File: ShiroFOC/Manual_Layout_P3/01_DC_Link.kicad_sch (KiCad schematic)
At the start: 19 parts, among them J101 AMASS XT60PW-M

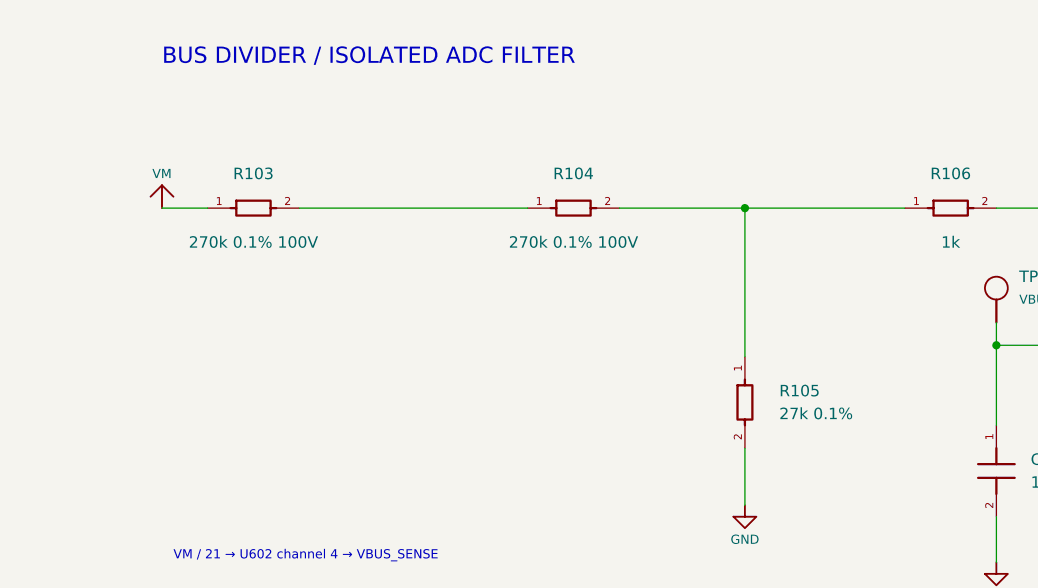
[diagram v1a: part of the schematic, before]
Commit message: STSPIN solder paste updated
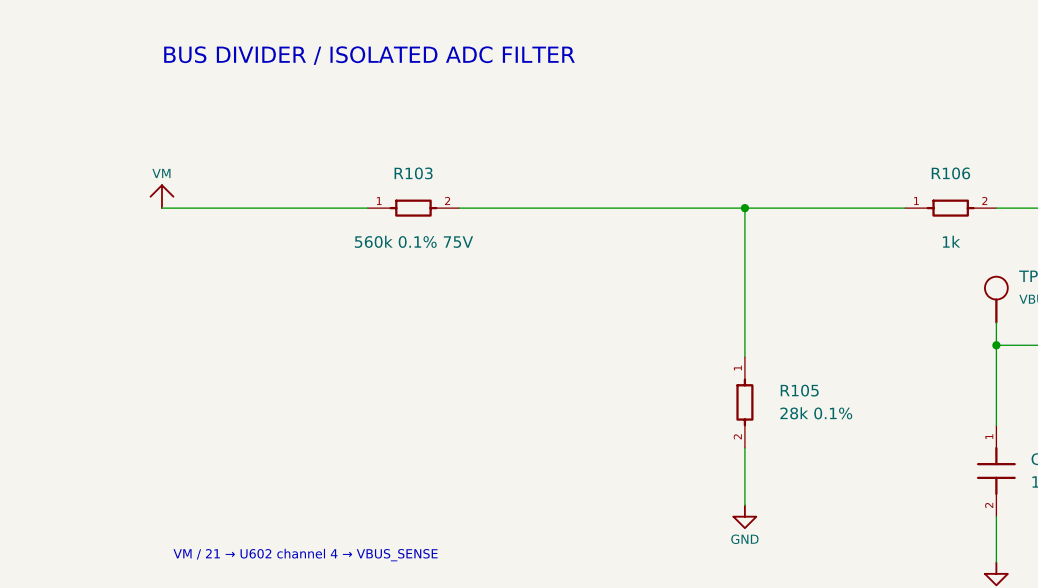
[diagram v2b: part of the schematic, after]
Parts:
- removed R104: 270k 0.1% 100V, Resistor_SMD:R_1206_3216Metric, symbol Manual:COMP_R104
- C108: Selection Note (none) -> ADC filter after U602 isolation. With 560k/28k divider and 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
- R103: value 270k 0.1% 100V -> 560k 0.1% 75V; footprint Resistor_SMD:R_1206_3216Metric -> Resistor_SMD:R_0603_1608Metric; LCSC (none) -> C719312; MPN (none) -> RT0603BRD07560KL; Manufacturer (none) -> Yageo; Procurement Select to specification: 270k 0.1% 100V; R_1206_3216Metric -> RT0603BRD07560KL; 560k 0.1%; 0603; 75V continuous rating; Rating See Value; generic low-voltage passives: R >=0.1 W / 50 V, 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 -> 0.1%; 25ppm/K; 0.1W; 75V continuous; Selection Note (none) -> Single upper resistor replaces R103/R104. Paired with R105=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
- R105: value 27k 0.1% -> 28k 0.1%; LCSC (none) -> C852686; MPN (none) -> RT0402BRD0728KL; Manufacturer (none) -> Yageo; Procurement 0402; preserve Value/tolerance requirements; exact part not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 -> RT0402BRD0728KL; 28k 0.1%; 0402; Rating See Value; generic low-voltage passives: R >=0.1 W / 50 V, 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 -> 0.1%; 25ppm/K; 0.0625W; 50V; Selection Note (none) -> Lower leg for R103=560k; preserves exact nominal division b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
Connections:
- net at R103.2: now also R105.1, R106.1
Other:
- moved on the sheet: R103
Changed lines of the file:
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@@
 	(wire
 		(pts
-			(xy 162.56 119.38) (xy 167.64 119.38)
+			(xy 162.56 119.38) (xy 185.42 119.38)
 		)
 		(stroke
@@
 	(wire
 		(pts
-			(xy 213.36 119.38) (xy 227.33 119.38)
+			(xy 195.58 119.38) (xy 227.33 119.38)
 		)
 		(stroke
@@
 		(pts
 			(xy 124.46 87.63) (xy 157.48 87.63)
-		)
-		(stroke
-			(width 0)
-			(type default)
-		)
-	)
-	(wire
-		(pts
-			(xy 177.8 119.38) (xy 203.2 119.38)
 		)
 		(stroke
@@
 			)
 		)
+		(property "Selection Note" "ADC filter after U602 isolation. With 560k/28k divider and R106=1k: nominal tau 277us, fc about 575Hz, neglecting switch resistance and ADC loading. Firmware must allow settling after mux enable."
+			(at 0 0 0)
+			(effects (font (size 1.27 1.27)) (hide yes))
+		)
 	)
 	(symbol
@@
 	(symbol
 		(lib_id "Manual:COMP_R103")
-		(at 172.72 119.38 0)
+		(at 190.5 119.38 0)
 		(unit 1)
 		(exclude_from_sim no)
@@
 		(dnp no)
 		(property "Reference" "R103"
-			(at 172.72 115.57 0)
-			(effects
-				(font
-					(size 1.27 1.27)
-				)
-			)
-		)
-		(property "Value" "270k 0.1% 100V"
-			(at 172.72 123.19 0)
-			(effects
-				(font
-					(size 1.27 1.27)
-				)
-			)
-		)
-		(property "Footprint" "Resistor_SMD:R_1206_3216Metric"
-			(at 172.72 123.19 0)
-			(effects
-				(font
-					(size 1.27 1.27)
-				)
-				(hide yes)
-			)
-		)
-		(property "Datasheet" ""
-			(at 172.72 123.19 0)
+			(at 190.5 115.57 0)
+			(effects
+				(font
+					(size 1.27 1.27)
+				)
+			)
+		)
+		(property "Value" "560k 0.1% 75V"
+			(at 190.5 123.19 0)
+			(effects
+				(font
+					(size 1.27 1.27)
+				)
+			)
+		)
+		(property "Footprint" "Resistor_SMD:R_0603_1608Metric"
+			(at 190.5 123.19 0)
+			(effects
+				(font
+					(size 1.27 1.27)
+				)
+				(hide yes)
+			)
+		)
+		(property "Datasheet" "https://www.yageogroup.com/component-documentation/download/specsheet/RT0603BRD07560KL"
+			(at 190.5 123.19 0)
 			(effects
 				(font
@@
 		)
 		(property "Description" ""
-			(at 172.72 119.38 0)
-			(effects
-				(font
-					(size 1.27 1.27)
-				)
-			)
-		)
-		(property "MPN" ""
-			(at 172.72 123.19 0)
+			(at 190.5 119.38 0)
+			(effects
+				(font
+					(size 1.27 1.27)
+				)
+			)
+		)
+		(property "MPN" "RT0603BRD07560KL"
+			(at 190.5 123.19 0)
 			(effects
 				(font
@@
 		)
 		(property "Assembly" "FIT"
-			(at 172.72 123.19 0)
-			(effects
-				(font
-					(size 1.27 1.27)
-				)
-				(hide yes)
-			)
-		)
-		(property "Procurement" "Select to specification: 270k 0.1% 100V; R_1206_3216Metric"
-			(at 172.72 123.19 0)
-			(effects
-				(font
-					(size 1.27 1.27)
-				)
-				(hide yes)
-			)
-		)
-		(property "Rating" "See Value; generic low-voltage passives: R >=0.1 W / 50 V, C >=16 V X7R unless specified"
-			(at 172.72 123.19 0)
+			(at 190.5 123.19 0)
+			(effects
+				(font
+					(size 1.27 1.27)
+				)
+				(hide yes)
+			)
+		)
+		(property "Procurement" "RT0603BRD07560KL; 560k 0.1%; 0603; 75V continuous rating"
+			(at 190.5 123.19 0)
+			(effects
+				(font
+					(size 1.27 1.27)
+				)
+				(hide yes)
+			)
+		)
+		(property "Rating" "0.1%; 25ppm/K; 0.1W; 75V continuous"
+			(at 190.5 123.19 0)
 			(effects
 				(font
@@
 				)
 			)
+		)
+		(property "Manufacturer" "Yageo"
+			(at 0 0 0)
+			(effects (font (size 1.27 1.27)) (hide yes))
+		)
+		(property "LCSC" "C719312"
+			(at 0 0 0)
+			(effects (font (size 1.27 1.27)) (hide yes))
+		)
+		(property "Selection Note" "Single upper resistor replaces R103/R104. Paired with R105=28k: VM/21, nominal 2.00V at 42V bus. About 40V and 2.86mW across R103 at 42V. Retain 0.1% for bus measurement accuracy used by firmware braking."
+			(at 0 0 0)
+			(effects (font (size 1.27 1.27)) (hide yes))
 		)
 	)
@@
 	)
 	(symbol
-		(lib_id "Manual:COMP_R104")
-		(at 208.28 119.38 0)
-		(unit 1)
-		(exclude_from_sim no)
-		(in_bom yes)
-		(on_board yes)
-		(dnp no)
-		(property "Reference" "R104"
-			(at 208.28 115.57 0)
-			(effects
-				(font
-					(size 1.27 1.27)
-				)
-			)
-		)
-		(property "Value" "270k 0.1% 100V"
-			(at 208.28 123.19 0)
-			(effects
-				(font
-					(size 1.27 1.27)
-				)
-			)
-		)
-		(property "Footprint" "Resistor_SMD:R_1206_3216Metric"
-			(at 208.28 123.19 0)
-			(effects
-				(font
-					(size 1.27 1.27)
-				)
-				(hide yes)
-			)
-		)
-		(property "Datasheet" ""
-			(at 208.28 123.19 0)
-			(effects
-				(font
-					(size 1.27 1.27)
-				)
-				(hide yes)
-			)
-		)
-		(property "Description" ""
-			(at 208.28 119.38 0)
-			(effects
-				(font
-					(size 1.27 1.27)
-				)
-			)
-		)
-		(property "MPN" ""
-			(at 208.28 123.19 0)
-			(effects
-				(font
-					(size 1.27 1.27)
-				)
-				(hide yes)
-			)
-		)
-		(property "Assembly" "FIT"
-			(at 208.28 123.19 0)
-			(effects
-				(font
-					(size 1.27 1.27)
-				)
-				(hide yes)
-			)
-		)
-		(property "Procurement" "Select to specification: 270k 0.1% 100V; R_1206_3216Metric"
-			(at 208.28 123.19 0)
-			(effects
-				(font
-					(size 1.27 1.27)
-				)
-				(hide yes)
-			)
-		)
-		(property "Rating" "See Value; generic low-voltage passives: R >=0.1 W / 50 V, C >=16 V X7R unless specified"
-			(at 208.28 123.19 0)
-			(effects
-				(font
-					(size 1.27 1.27)
-				)
-				(hide yes)
-			)
-		)
-		(pin "1"
-		)
-		(pin "2"
-		)
-		(instances
-			(project "ShiroFOC_Manual"
-				(path "/2c8b7510-9664-4afd-8f00-ac42aa791be9/302dc34a-7561-4149-81f0-6edd60941159"
-					(reference "R104")
-					(unit 1)
-				)
-			)
-		)
-	)
-	(symbol
 		(lib_id "Manual:COMP_R105")
 		(at 227.33 140.97 0)
@@
 			)
 		)
-		(property "Value" "27k 0.1%"
+		(property "Value" "28k 0.1%"
 			(at 231.14 142.24 0)
 			(effects
@@
 			)
 		)
-		(property "Datasheet" ""
+		(property "Datasheet" "https://www.yageogroup.com/content/datasheet/asset/file/PYU-RT_1-TO-0-01_ROHS_L"
 			(at 231.14 142.24 0)
 			(effects
@@
 			)
 		)
-		(property "MPN" ""
+		(property "MPN" "RT0402BRD0728KL"
 			(at 231.14 142.24 0)
 			(effects
@@
 			)
 		)
-		(property "Procurement" "0402; preserve Value/tolerance requirements; exact part not selected"
+		(property "Procurement" "RT0402BRD0728KL; 28k 0.1%; 0402"
 			(at 231.14 142.24 0)
 			(effects
@@
 			)
 		)
-		(property "Rating" "See Value; generic low-voltage passives: R >=0.1 W / 50 V, C >=16 V X7R unless specified"
+		(property "Rating" "0.1%; 25ppm/K; 0.0625W; 50V"
 			(at 231.14 142.24 0)
 			(effects
@@
 			)
 		)
-	)
+		(property "Manufacturer" "Yageo"
+			(at 0 0 0)
+			(effects (font (size 1.27 1.27)) (hide yes))
+		)
+		(property "LCSC" "C852686"
+			(at 0 0 0)
+			(effects (font (size 1.27 1.27)) (hide yes))
+		)
+		(property "Selection Note" "Lower leg for R103=560k; preserves exact nominal division by 21. Resistor-tolerance-only bus error about +/-0.08V at 42V; ADC, reference, leakage and temperature errors add."
+			(at 0 0 0)
+			(effects (font (size 1.27 1.27)) (hide yes))
+		)
+	)

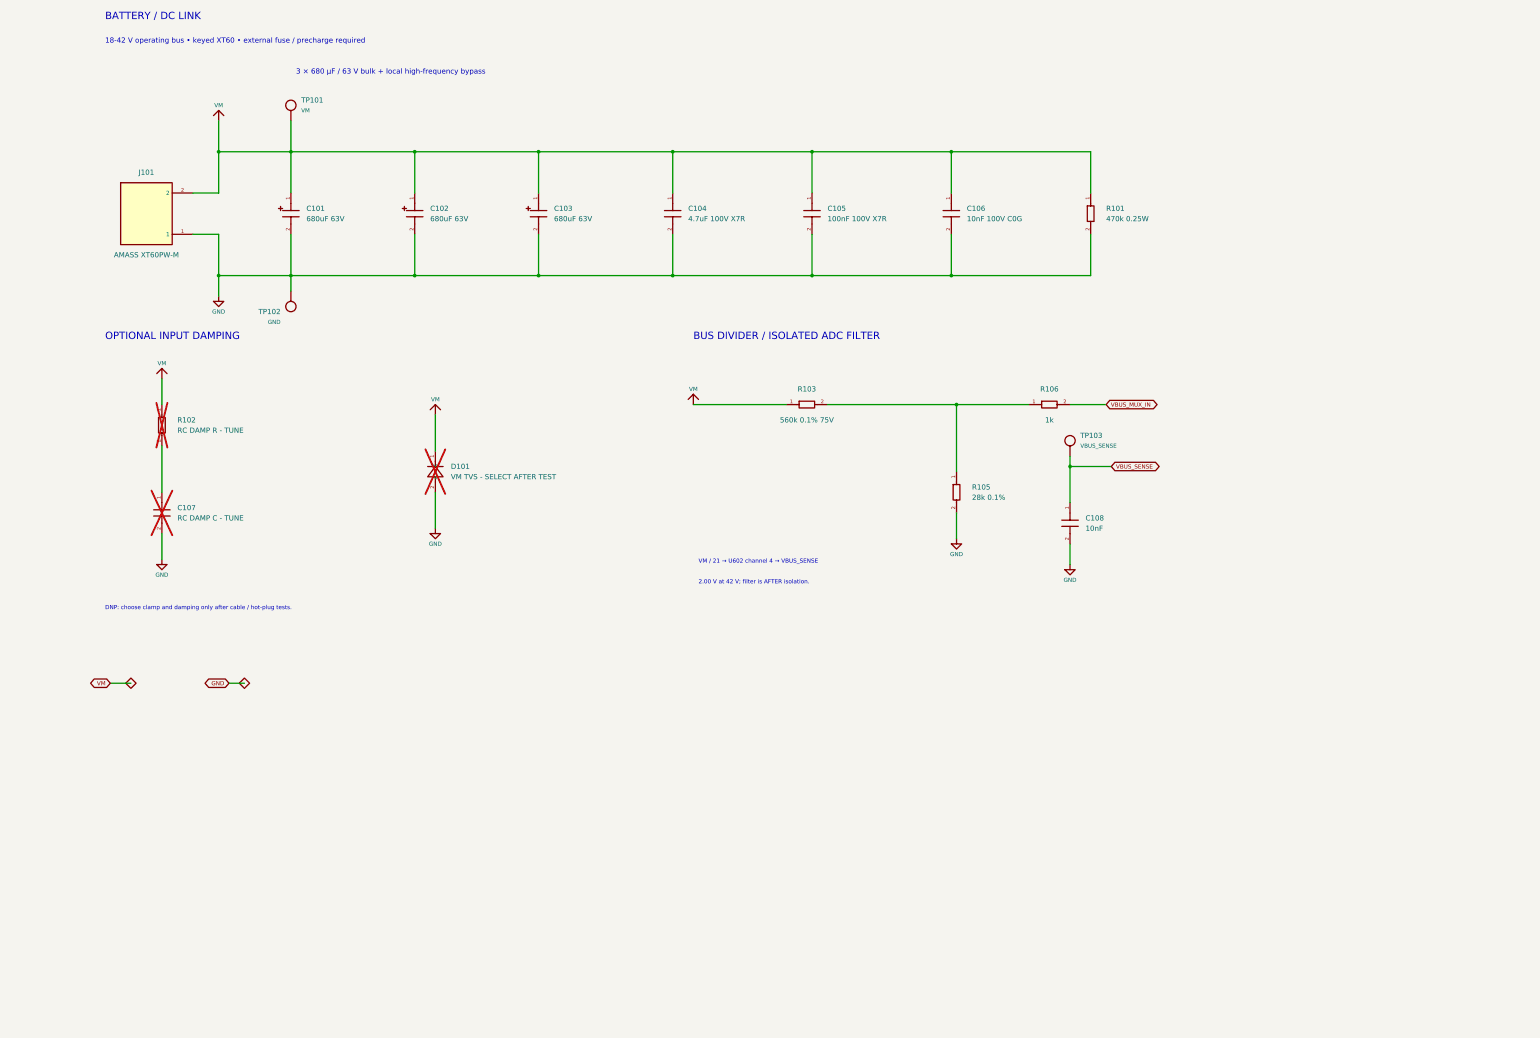
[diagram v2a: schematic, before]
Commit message: usb and pwr mux
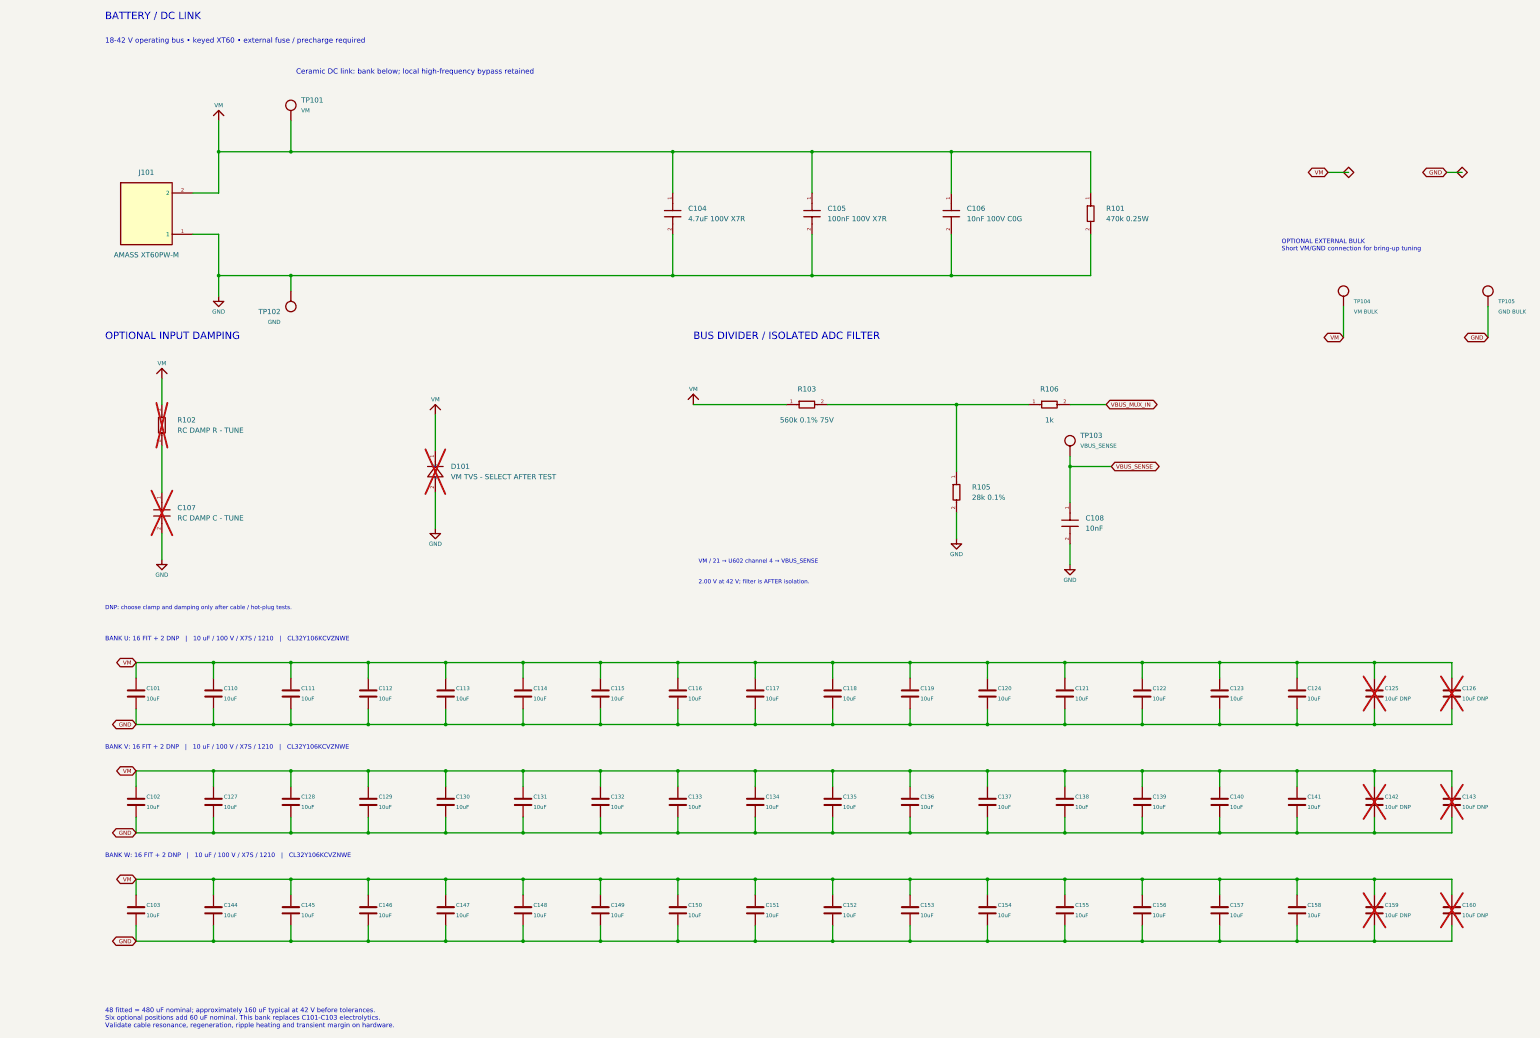
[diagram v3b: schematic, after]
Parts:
- added C110, C111, C112, C113, C114, C115, C116, C117, C118, C119, C120, C121, C122, C123, C124, C127, C128, C129, C130, C131, C132, C133, C134, C135, C136, C137, C138, C139, C140, C141, C144, C145, C146, C147, C148, C149, C150, C151, C152, C153, C154, C155, C156, C157, C158: 10uF, Capacitor_SMD:C_1210_3225Metric, symbol Device:C
- added C125, C126, C142, C143, C159, C160: 10uF DNP, Capacitor_SMD:C_1210_3225Metric, symbol Device:C
- added TP104: VM BULK, TestPoint:TestPoint_Pad_D3.0mm, symbol Manual:COMP_TP101
- added TP105: GND BULK, TestPoint:TestPoint_Pad_D3.0mm, symbol Manual:COMP_TP101
- C101: value 680uF 63V -> 10uF; footprint Manual:Panasonic_EEVFK_K16_18x16.5 -> Capacitor_SMD:C_1210_3225Metric; symbol Manual:COMP_C101 -> Device:C; BOM Comments (none) -> Prototype ceramic DC link. Approximately 3.3 uF typical at 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; Bank (none) -> U; Dielectric (none) -> X7S; LCSC (none) -> C3840810; MPN EEVFK1J681M -> CL32Y106KCVZNWE; Manufacturer (none) -> Samsung Electro-Mechanics; Rating See Value; generic low-voltage passives: R >=0.1 W / 50 V, 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 -> (none); Tolerance (none) -> 10%; Voltage Rating (none) -> 100 V
- C102: value 680uF 63V -> 10uF; footprint Manual:Panasonic_EEVFK_K16_18x16.5 -> Capacitor_SMD:C_1210_3225Metric; symbol Manual:COMP_C102 -> Device:C; BOM Comments (none) -> Prototype ceramic DC link. Approximately 3.3 uF typical at 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; Bank (none) -> V; Dielectric (none) -> X7S; LCSC (none) -> C3840810; MPN EEVFK1J681M -> CL32Y106KCVZNWE; Manufacturer (none) -> Samsung Electro-Mechanics; Rating See Value; generic low-voltage passives: R >=0.1 W / 50 V, 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 -> (none); Tolerance (none) -> 10%; Voltage Rating (none) -> 100 V
- C103: value 680uF 63V -> 10uF; footprint Manual:Panasonic_EEVFK_K16_18x16.5 -> Capacitor_SMD:C_1210_3225Metric; symbol Manual:COMP_C103 -> Device:C; BOM Comments (none) -> Prototype ceramic DC link. Approximately 3.3 uF typical at 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; Bank (none) -> W; Dielectric (none) -> X7S; LCSC (none) -> C3840810; MPN EEVFK1J681M -> CL32Y106KCVZNWE; Manufacturer (none) -> Samsung Electro-Mechanics; Rating See Value; generic low-voltage passives: R >=0.1 W / 50 V, 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 -> (none); Tolerance (none) -> 10%; Voltage Rating (none) -> 100 V
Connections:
- net GND: now also C110.2, C111.2, C112.2, C113.2, C114.2, C115.2, C116.2, C117.2, C118.2, C119.2, C120.2, C121.2, C122.2, C123.2, C124.2, C125.2, C126.2, C127.2, C128.2, C129.2, C130.2, C131.2, C132.2, C133.2, C134.2, C135.2, C136.2, C137.2, C138.2, C139.2, C140.2, C141.2, C142.2, C143.2, C144.2, C145.2, C146.2, C147.2, C148.2, C149.2, C150.2, C151.2, C152.2, C153.2, C154.2, C155.2, C156.2, C157.2, C158.2, C159.2, C160.2, TP105.1
- net VM: now also C110.1, C111.1, C112.1, C113.1, C114.1, C115.1, C116.1, C117.1, C118.1, C119.1, C120.1, C121.1, C122.1, C123.1, C124.1, C125.1, C126.1, C127.1, C128.1, C129.1, C130.1, C131.1, C132.1, C133.1, C134.1, C135.1, C136.1, C137.1, C138.1, C139.1, C140.1, C141.1, C142.1, C143.1, C144.1, C145.1, C146.1, C147.1, C148.1, C149.1, C150.1, C151.1, C152.1, C153.1, C154.1, C155.1, C156.1, C157.1, C158.1, C159.1, C160.1, TP104.1
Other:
- note added: "48 fitted = 480 uF nominal; approximately 160 uF typical at 42 V before tolerances. Six optional positions add 60 uF nominal. This bank replaces C101-C103 electrolytics. Validate cable resonance, regeneration, ripple heating and transient margin on hardware."
- note added: "BANK U: 16 FIT + 2 DNP | 10 uF / 100 V / X7S / 1210 | CL32Y106KCVZNWE"
- note added: "BANK V: 16 FIT + 2 DNP | 10 uF / 100 V / X7S / 1210 | CL32Y106KCVZNWE"
- note added: "BANK W: 16 FIT + 2 DNP | 10 uF / 100 V / X7S / 1210 | CL32Y106KCVZNWE"
- note added: "Ceramic DC link: bank below; local high-frequency bypass retained"
- note added: "OPTIONAL EXTERNAL BULK Short VM/GND connection for bring-up tuning"
- note removed: "3 × 680 µF / 63 V bulk + local high-frequency bypass"
